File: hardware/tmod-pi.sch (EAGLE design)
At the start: 23 parts, among them J1 RASPBERRYPI-40-PIN-GPIO_PTH, J2 HAB-EXP, J3 GROVE, J4 SMA_EDGE, U1 DNP (74AHC1G125), U2 DNP (PCA9306), U3 DNP (74AHC1G125), U4 RA01

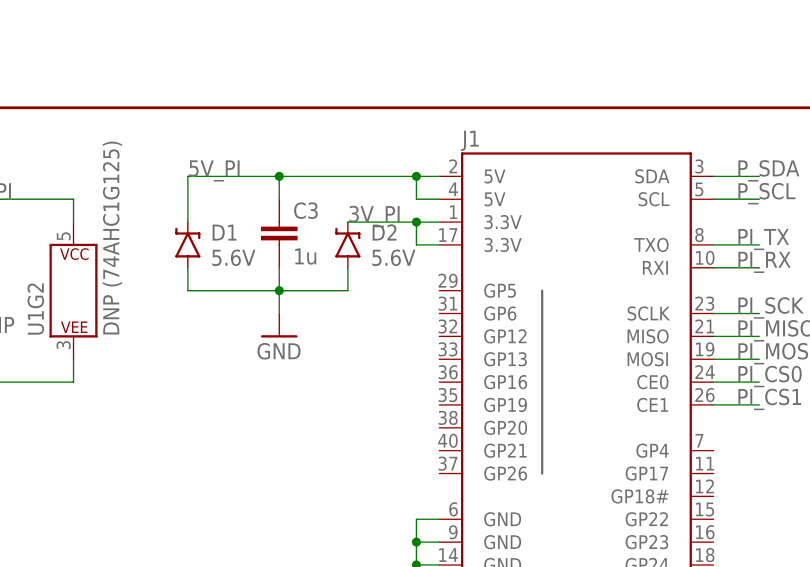
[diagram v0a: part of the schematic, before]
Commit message: Finalize routing on the Raspberry PI-compatible Application Module. 5V net is not routed, but is not used on the module so not required.
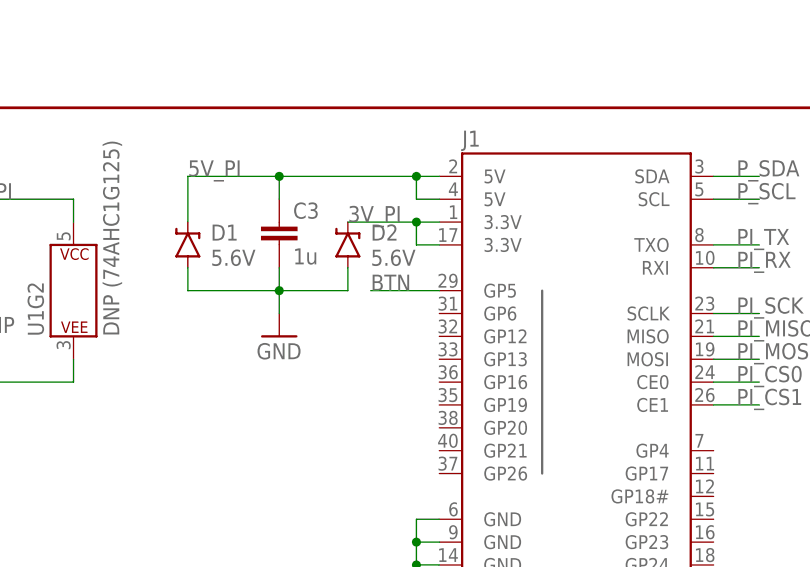
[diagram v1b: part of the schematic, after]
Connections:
- net BTN: now also J1.GP5
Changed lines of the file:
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@@
 <label x="236.22" y="93.98" size="1.778" layer="95"/>
+</segment>
+<segment>
+<pinref part="J1" gate="G$1" pin="GP5"/>
+<wire x1="73.66" y1="119.38" x2="81.28" y2="119.38" width="0.1524" layer="91"/>
+<label x="73.66" y="119.38" size="1.778" layer="95"/>
 </segment>
 </net>
